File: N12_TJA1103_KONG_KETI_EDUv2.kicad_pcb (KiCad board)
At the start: 2 copper layers, 33 x 57 mm, 65 parts, among them IC1 TJA1103AHN, J1 Conn_02x02_Odd_Even, J2 Conn_02x11_Odd_Even, J3 9-2304372-9, J4 E6S20A-40MT5-Z, Q1 FDN340P, Q2 BSS138, SW2 SW-DIP-ANGLED DS03-254-02BE, Y1 Crystal_GND24_Small

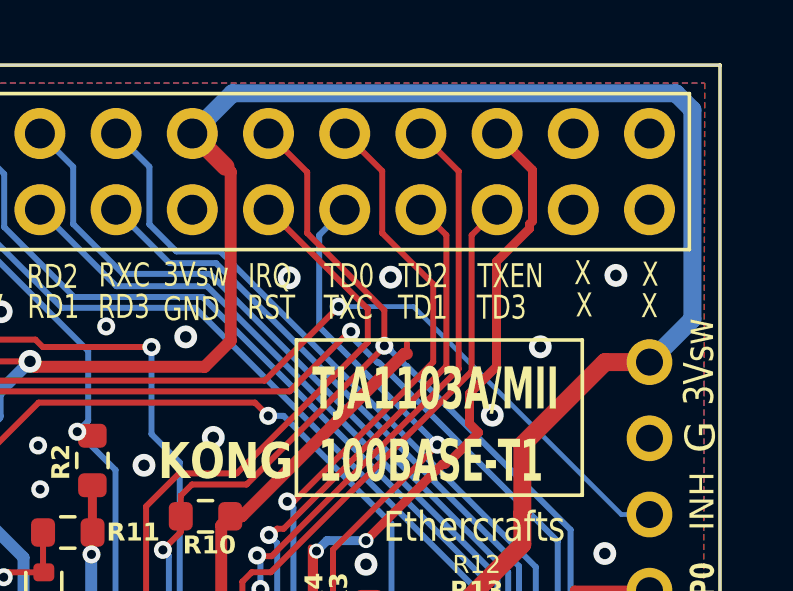
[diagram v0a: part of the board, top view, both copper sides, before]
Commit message: chore: add KETI silkscreen and downloaded 3D models
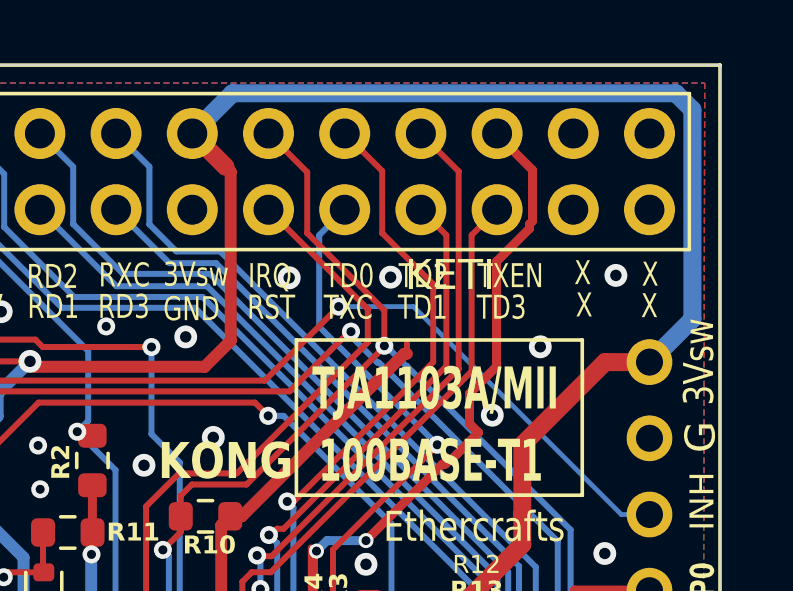
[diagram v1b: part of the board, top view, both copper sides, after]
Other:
- board text added: "KETI"
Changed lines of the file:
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@@
 		)
 		(embedded_fonts no)
-		(model "C:/KiCad/ext3d/5680F5_5_LED_DUAL_STACK.stp"
+		(model "${KIPRJMOD}/lib/3d/5680F5_5/5680F5_5.stp"
 			(offset
 				(xyz 0 -4.5 4.5)
@@
 		)
 		(embedded_fonts no)
-		(model "DS03-254-02BE.stp"
+		(model "${KIPRJMOD}/lib/3d/DS03-254-02BE/DS03-254-02BE.stp"
 			(offset
 				(xyz 0 0 0)
@@
 			)
 		)
-		(model "C:/KiCad/extLib/LIB_DS03-254-02BE/DS03-254-02BE/3D/DS03-254-02BE.stp"
+		(model "${KIPRJMOD}/lib/3d/DS03-254-02BE/DS03-254-02BE.stp"
 			(offset
 				(xyz -2 -0.7 0)
@@
 		)
 		(embedded_fonts no)
-		(model "ACT45L-201-2P-TL000.stp"
+		(model "${KIPRJMOD}/lib/3d/ACT45L-201-2P-TL000/ACT45L-201-2P-TL000.stp"
 			(offset
 				(xyz 0.2 -4.499999932 1.899999948)
@@
 		)
 		(embedded_fonts no)
-		(model "C:/KiCad/ext3d/5680F5_5_LED_DUAL_STACK.stp"
+		(model "${KIPRJMOD}/lib/3d/5680F5_5/5680F5_5.stp"
 			(offset
 				(xyz 0 -4.5 4.5)
@@
 		)
 	)
+	(gr_text "KETI"
+		(at 24 7 0)
+		(layer "F.SilkS")
+		(effects
+			(font
+				(size 1 1)
+				(thickness 0.15)
+			)
+		)
+	)
